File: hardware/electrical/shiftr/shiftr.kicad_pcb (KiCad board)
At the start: 2 copper layers, 6 parts, among them J1 2171750001, J2 PJ-002AH, J3 SJ1-3523N

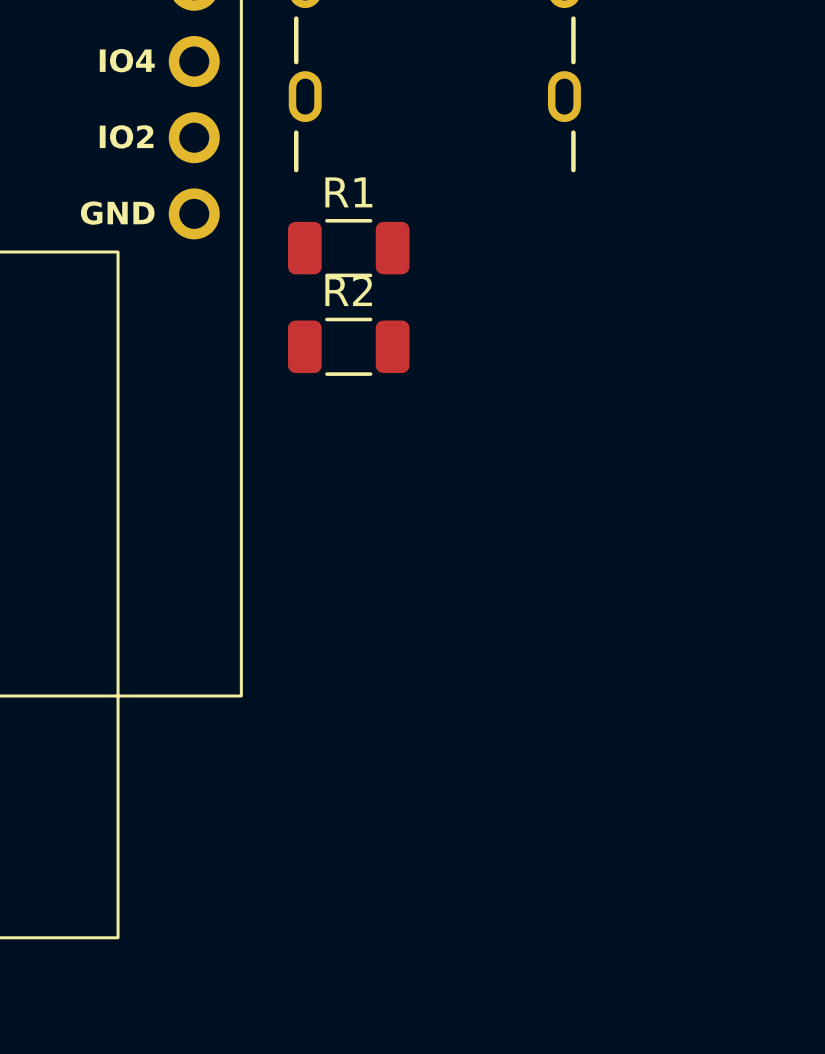
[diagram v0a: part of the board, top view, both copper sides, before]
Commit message: flesh out more of the 48v->5v conversion
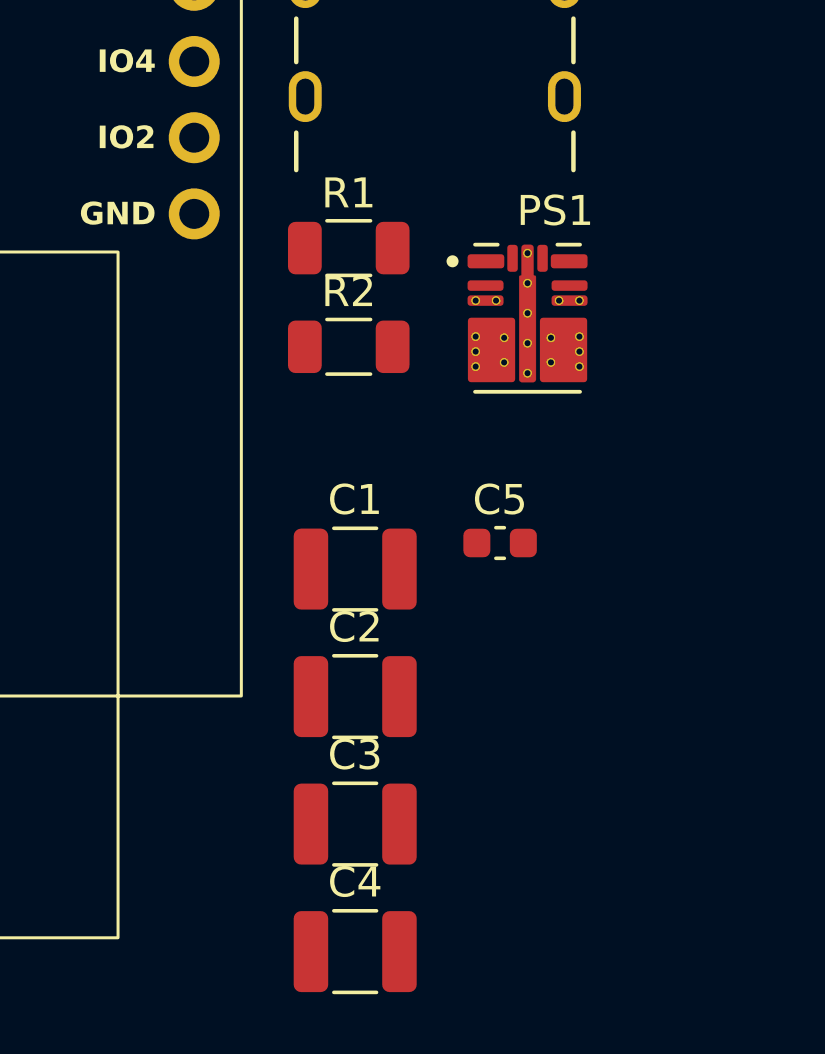
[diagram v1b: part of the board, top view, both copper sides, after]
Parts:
- added C1: 10uF, Capacitor_SMD:C_1210_3225Metric, F.Cu at (192.5, 102.2)
- added C2: 0.1uF, Capacitor_SMD:C_1210_3225Metric, F.Cu at (192.5, 106.5)
- added C3: 2.2uF, Capacitor_SMD:C_1210_3225Metric, F.Cu at (192.5, 110.8)
- added C4: 2.2uF, Capacitor_SMD:C_1210_3225Metric, F.Cu at (192.5, 115.0)
- added C5: 1uF, Capacitor_SMD:C_0603_1608Metric, F.Cu at (197.4, 101.4)
- added PS1: TPSM365R6V5RDNR, footprint_library:TPSM365R6V5RDNR, F.Cu at (198.3, 94.0)
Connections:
- J2 pad 1: unconnected-(J2-Pad1) -> 48V
- J2 pad 2: unconnected-(J2-Pad2) -> GND
- J2 pad 3: unconnected-(J2-Pad3) -> GND
- SOC1 pad 12: unconnected-(SOC1-5V-Pad12) -> 5V

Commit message: add shift button nets, pull down resistors
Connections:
- J3 pad 1: unconnected-(J3-Pad1) -> GND
- J3 pad 2: unconnected-(J3-Pad2) -> /SHIFT_DOWN
- J3 pad 3: unconnected-(J3-Pad3) -> /SHIFT_UP
- SOC1 pad 11: unconnected-(SOC1-GND-Pad11) -> GND
- SOC1 pad 15: unconnected-(SOC1-IO2-Pad15) -> /SHIFT_UP
- SOC1 pad 16: unconnected-(SOC1-IO4-Pad16) -> /SHIFT_DOWN
- SOC1 pad 2: unconnected-(SOC1-GND-Pad2) -> GND
- SOC1 pad 23: unconnected-(SOC1-GND-Pad23) -> GND
- SOC1 pad 9: unconnected-(SOC1-GND-Pad9) -> GND

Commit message: route traces
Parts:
- added C6: 10uF, Capacitor_SMD:C_1210_3225Metric, F.Cu at (176.5, 90.4)
- added C7: 1uF, Capacitor_SMD:C_0603_1608Metric, F.Cu at (177.2, 87.0)
- added H1: ~, footprint_library:Hole-3mm, F.Cu at (124.3, 106.0)
- added H2: ~, footprint_library:Hole-3mm, F.Cu at (147.4, 106.2)
- added H3: ~, footprint_library:Hole-3mm, F.Cu at (171.9, 61.2)
- added H4: ~, footprint_library:Hole-3mm, F.Cu at (129.0, 79.0)
- added R3: R10K, Resistor_SMD:R_1206_3216Metric, F.Cu at (142.0, 95.5)
- added R4: R10K, Resistor_SMD:R_1206_3216Metric, F.Cu at (132.0, 95.5)
- added R5: R10K, Resistor_SMD:R_1206_3216Metric, F.Cu at (122.5, 85.7)
- added R7: R10K, Resistor_SMD:R_1206_3216Metric, F.Cu at (123.5, 67.5)
- added S1: SDA01H1SBD, footprint_library:SW_SDA01H1SBD, F.Cu at (131.5, 69.0)
- moved J3 76.8 mm to (135.5, 106.5)
- moved SOC1 69.4 mm to (106.4, 82.5)
- moved J2 52.6 mm to (150.0, 104.2), turned to -90 degrees
- moved C5 47.9 mm to (156.3, 76.7)
- moved C2 43.1 mm to (154.0, 87.2), turned to 180 degrees
- moved C4 42.8 mm to (160.0, 87.2)
- moved PS1 42.7 mm to (157.4, 81.5), turned to 90 degrees
- moved C1 39.8 mm to (154.0, 92.2), turned to 180 degrees
- moved C3 37.4 mm to (160.1, 92.2)
- moved J1 30.7 mm to (173.8, 111.1)
- moved R1 22.4 mm to (170.8, 97.6), turned to 90 degrees
- moved R2 17.7 mm to (174.8, 97.6), turned to 90 degrees
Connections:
- C1 pad 2: Net-(PS1-EN) -> GND
- C2 pad 2: Net-(PS1-EN) -> GND
- J1 pad A9: /5V_USB -> 5V
- J1 pad B9: /5V_USB -> 5V
- PS1 pad 2: Net-(PS1-EN) -> 48V
- PS1 pad 3: Net-(PS1-EN) -> 48V
- SOC1 pad 18: unconnected-(SOC1-IO12-Pad18) -> Net-(SOC1-IO12)
- SOC1 pad 24: unconnected-(SOC1-IO0-Pad24) -> Net-(SOC1-IO0)
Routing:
- net 5V: track 0.00 -> 194.6 mm
- net GND: track 0.00 -> 61.7 mm, vias 0 -> 17
- net /SHIFT_DOWN: track 0.00 -> 31.3 mm
- net /SHIFT_UP: track 0.00 -> 20.2 mm
- net 48V: track 0.00 -> 17.6 mm
- net Net-(SOC1-IO0): track 0.00 -> 9.52 mm
- net Net-(J1-CC1): track 0.00 -> 6.58 mm
- net Net-(J1-CC2): track 0.00 -> 5.74 mm
- net Net-(SOC1-IO12): track 0.00 -> 4.66 mm
- net unconnected-(SOC1-GND-Pad14): track 0.00 -> 3.14 mm, vias 0 -> 1
- net Net-(PS1-VCC): track 0.00 -> 3.12 mm
- added copper zone on B.Cu, net GND
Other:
- board outline added: 86.1 x 55 mm
- board text added: "PROG"

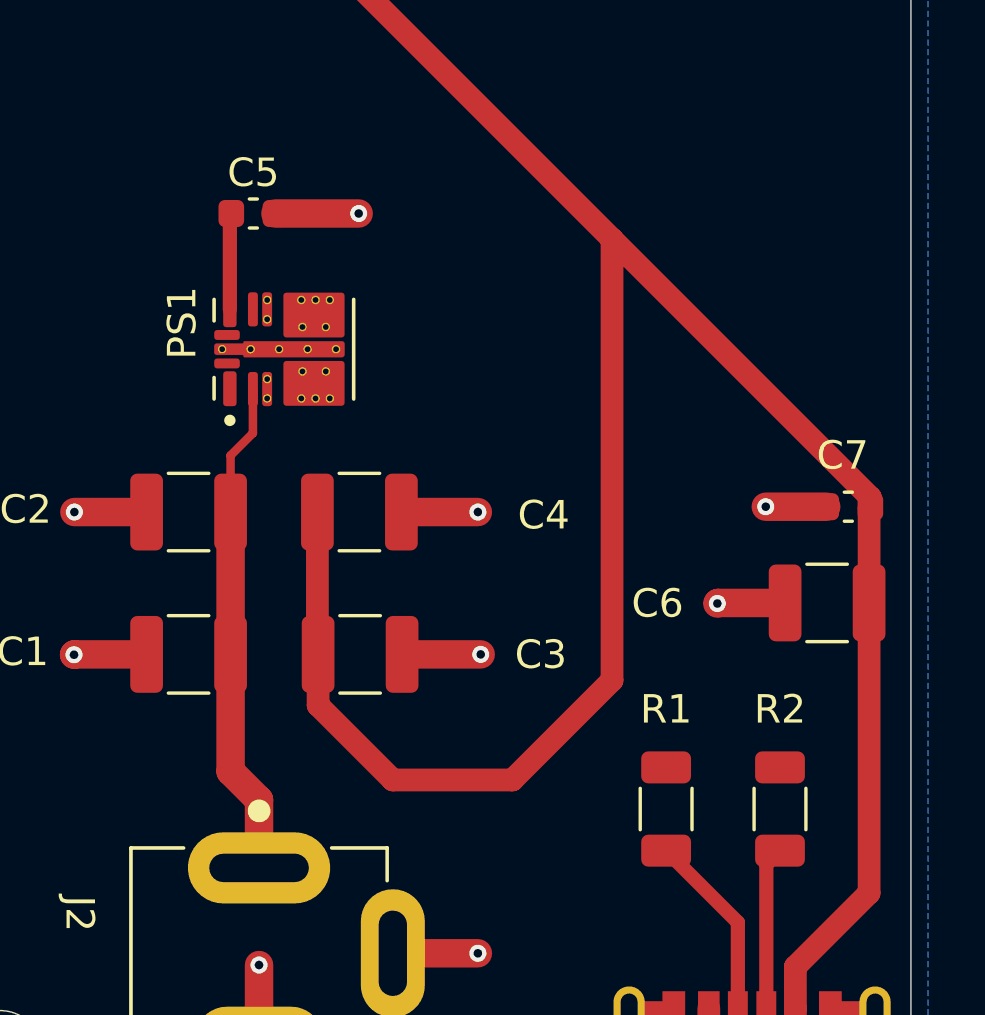
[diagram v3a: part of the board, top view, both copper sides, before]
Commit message: finish up routing, wt32 now on headers
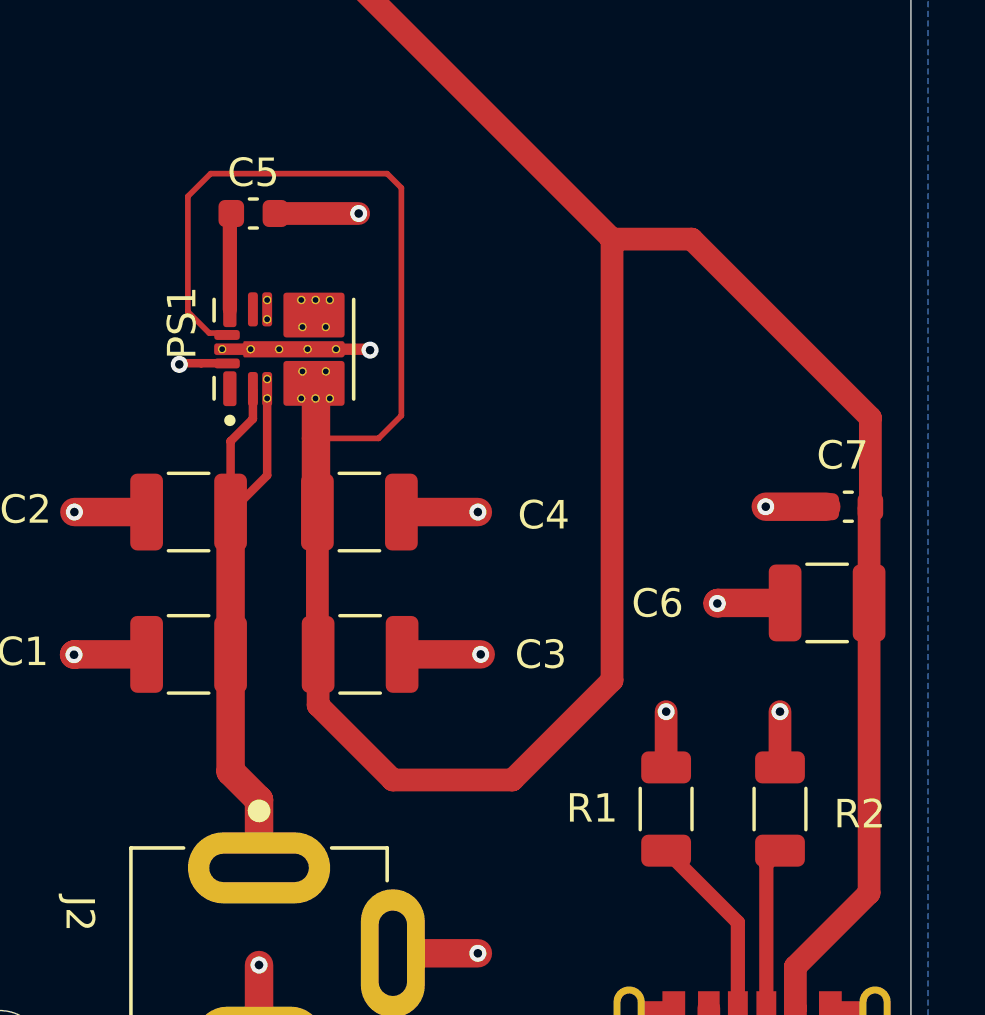
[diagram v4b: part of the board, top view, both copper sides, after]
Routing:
- net 5V: track 194.6 -> 225.4 mm
- net GND: track 61.7 -> 68.5 mm, vias 17 -> 21
- net 48V: track 17.6 -> 22.1 mm

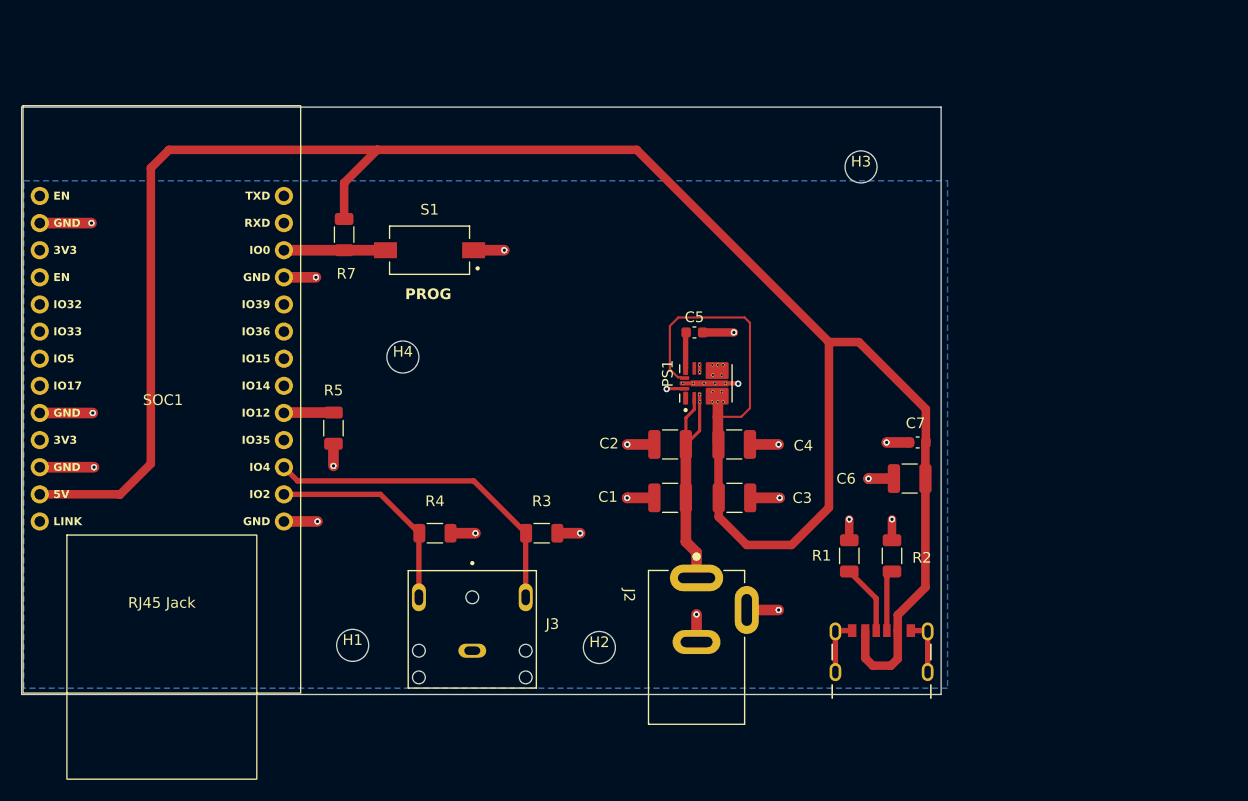
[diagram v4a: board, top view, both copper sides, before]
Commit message: add programming pinheader
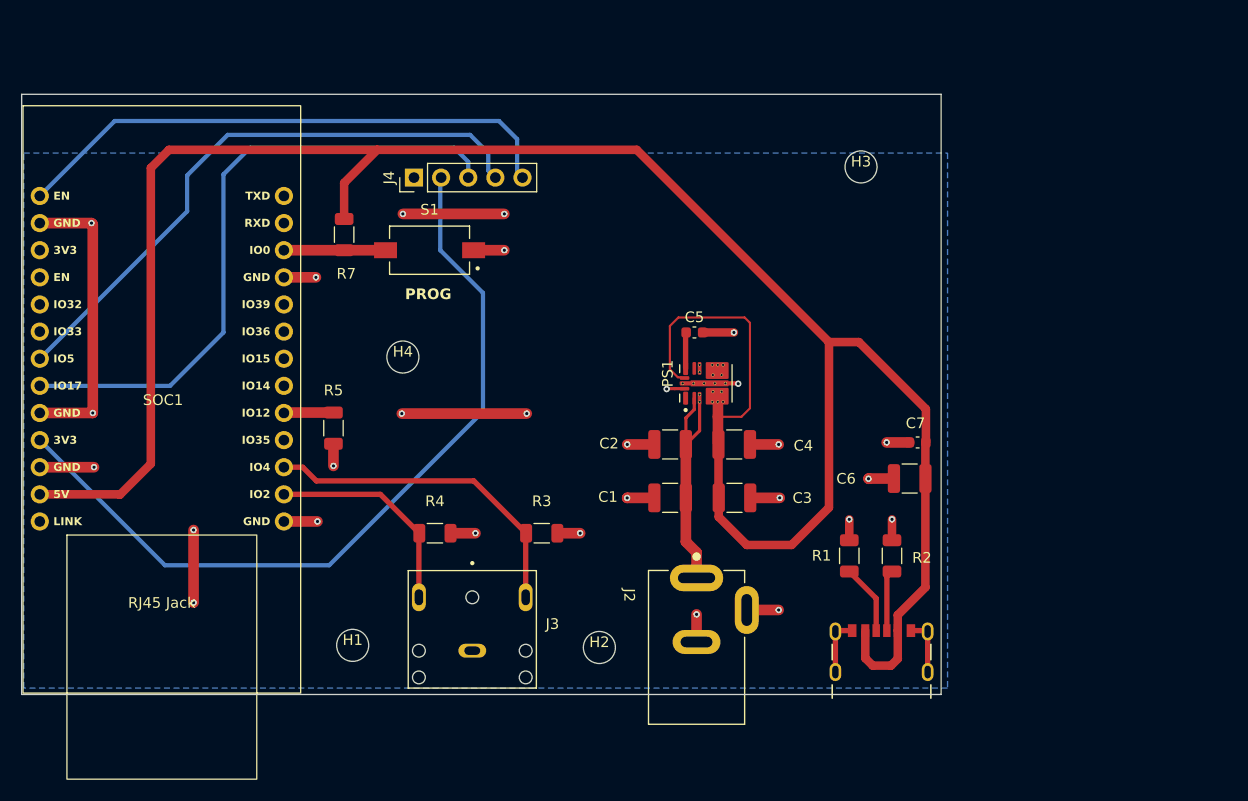
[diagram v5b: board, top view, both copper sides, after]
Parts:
- added J4: Conn_01x05_Pin, Connector_PinHeader_2.54mm:PinHeader_1x05_P2.54mm_Vertical, F.Cu at (130.0, 62.2)
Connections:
- SOC1 pad 1: unconnected-(SOC1-EN-Pad1) -> /EN
- SOC1 pad 10: unconnected-(SOC1-3V3-Pad10) -> /3V3
- SOC1 pad 14: unconnected-(SOC1-GND-Pad14) -> GND
- SOC1 pad 7: unconnected-(SOC1-RXD-Pad7) -> /RXD
- SOC1 pad 8: unconnected-(SOC1-TXD-Pad8) -> /TXD
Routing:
- net /3V3: track 0.00 -> 75.9 mm
- net /TXD: track 0.00 -> 60.1 mm
- net /RXD: track 0.00 -> 55.9 mm
- net /EN: track 0.00 -> 52.1 mm
- net GND: track 68.5 -> 117.5 mm, vias 21 -> 28
- net unconnected-(SOC1-GND-Pad14): track 3.14 -> 0.00 mm, vias 1 -> 0
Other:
- board size 86.1 x 55 mm -> 86.1 x 56.2 mm

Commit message: update some traces
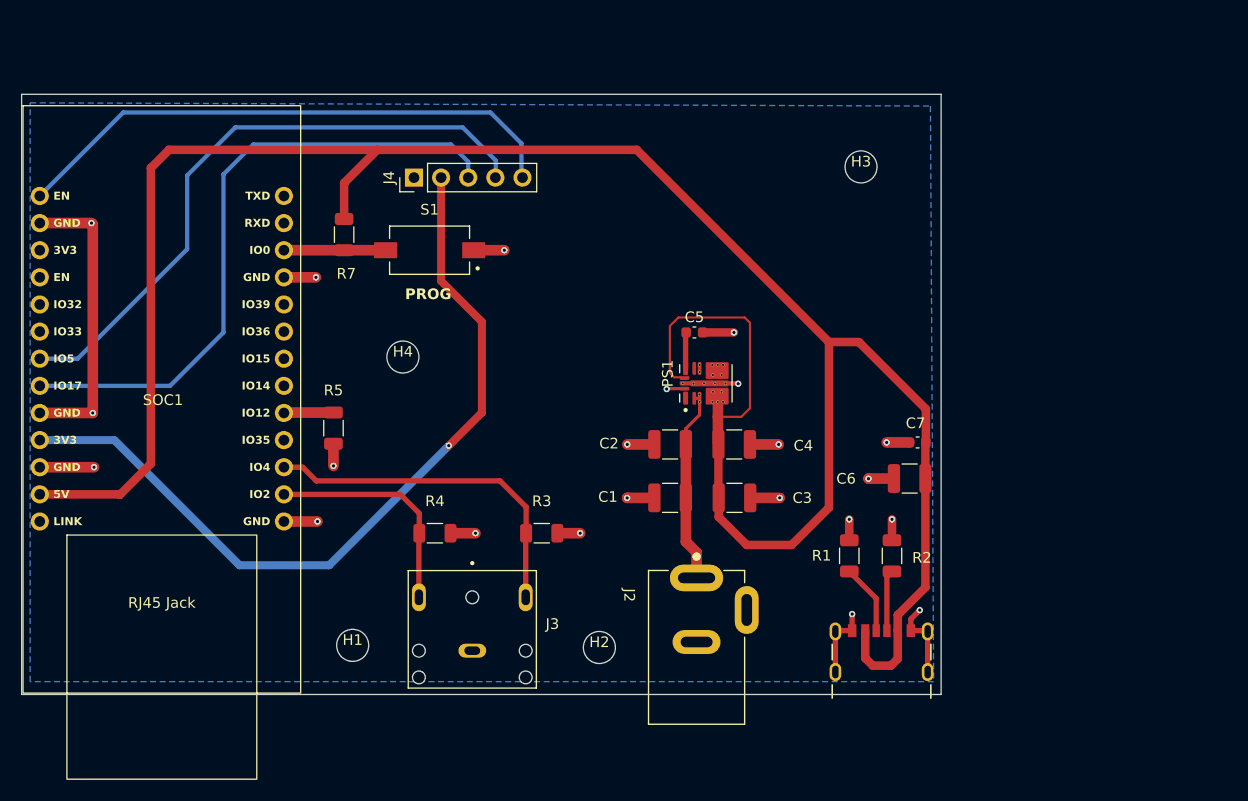
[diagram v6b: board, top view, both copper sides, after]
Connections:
- PS1 pad 3_1: (no net) -> 48V
- PS1 pad 3_2: (no net) -> 48V
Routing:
- net GND: track 117.5 -> 87.8 mm, vias 28 -> 22
- net 48V: track 22.1 -> 17.9 mm
- net /RXD: track 55.9 -> 58.6 mm
- net /SHIFT_DOWN: track 31.3 -> 32.7 mm
- net /SHIFT_UP: track 20.2 -> 21.3 mm
- net /EN: track 52.1 -> 52.8 mm
- net /3V3: vias 0 -> 1
